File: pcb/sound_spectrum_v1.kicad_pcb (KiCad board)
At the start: 4 copper layers, 85.6 x 54 mm, 33 parts, among them IC1-L1 ICS-43432, IC2-R1 ICS-43432, J1 SWD_CONN, J2 Conn_02x10_Counter_Clockwise, P1 USB_C_Plug_USB2.0, SW2 SW_DPST_x2, U1 STM32G473CBTx, U2 AP2112K-3.3, U3 USBLC6-2SC6, Y2 SG-210STF 48.0000ML5

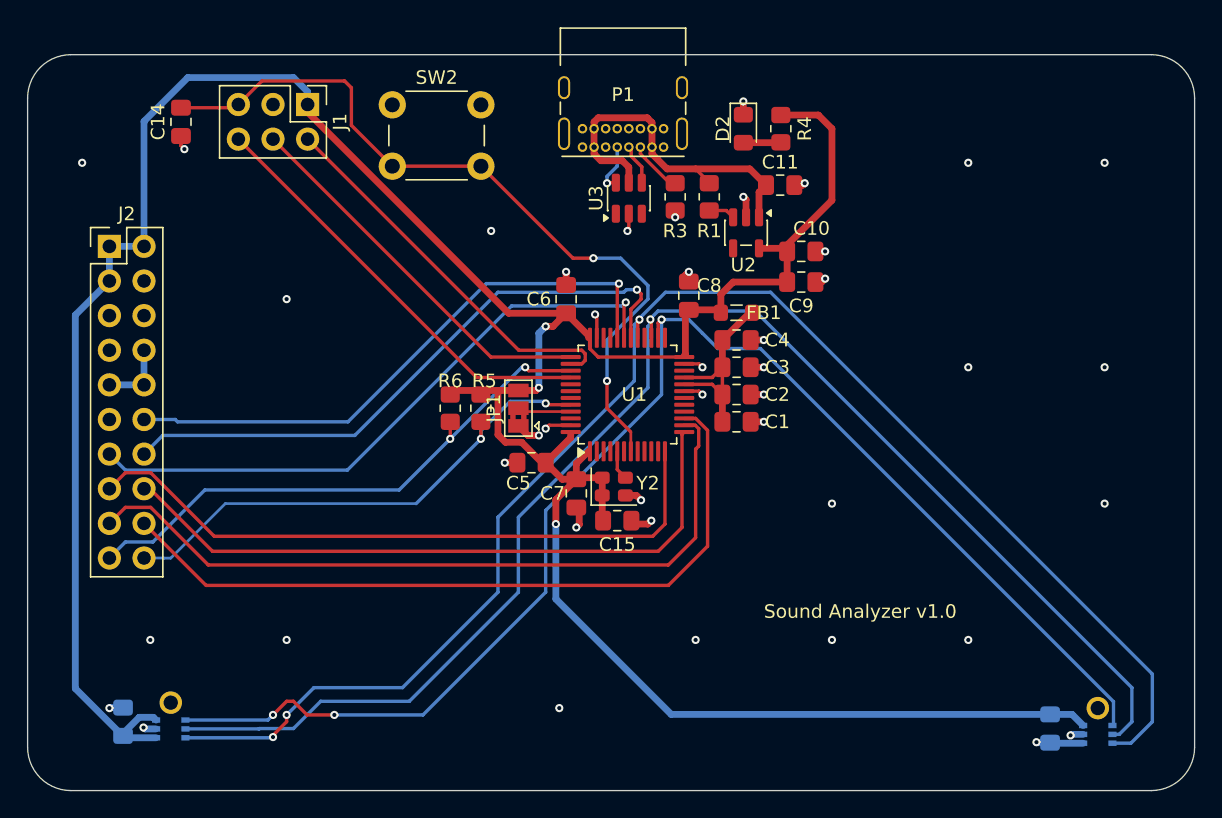
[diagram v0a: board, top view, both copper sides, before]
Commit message: feat: add mounting holes
chore: change usb c receptor

chore: align microphones
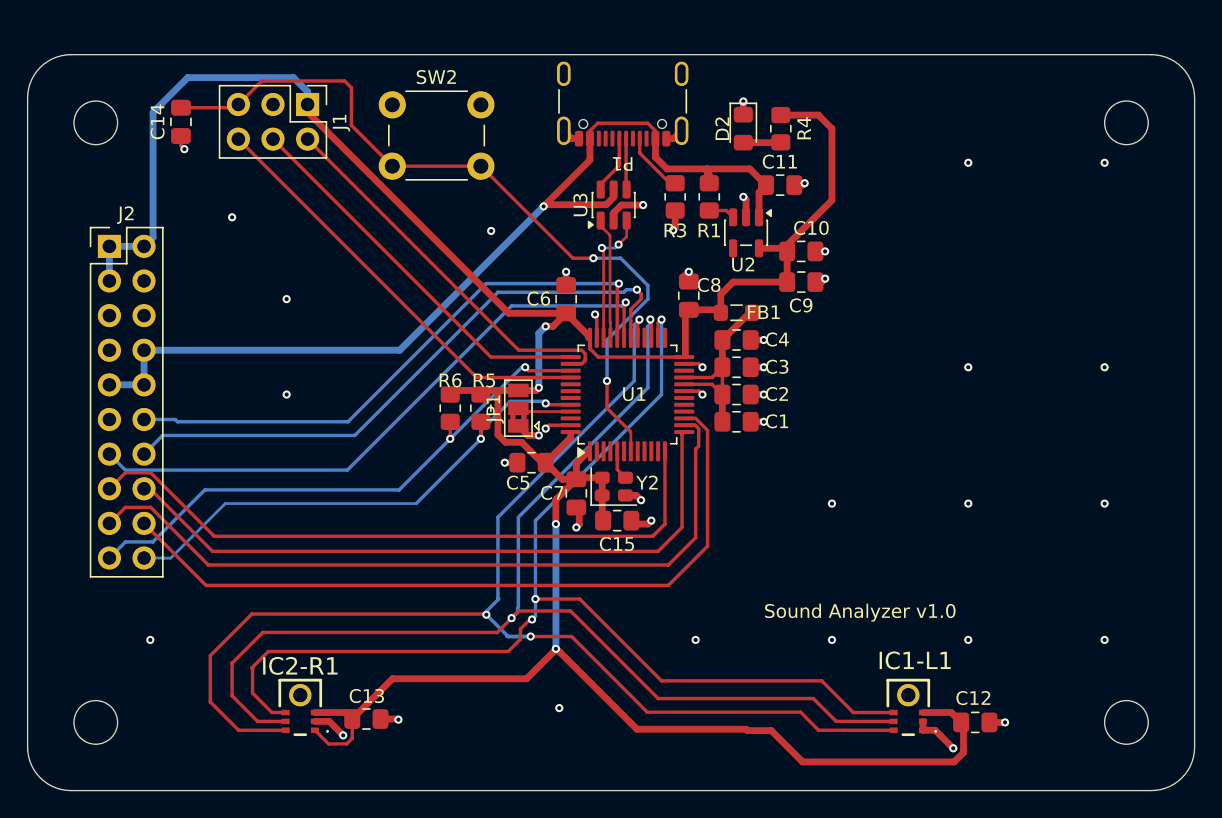
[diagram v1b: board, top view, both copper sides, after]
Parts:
- added H1: MountingHole, MountingHole:MountingHole_3.2mm_M3_DIN965, F.Cu at (181.6, 97.1)
- added H2: MountingHole, MountingHole:MountingHole_3.2mm_M3_DIN965, F.Cu at (106.0, 97.1)
- added H3: MountingHole, MountingHole:MountingHole_3.2mm_M3_DIN965, F.Cu at (181.6, 141.1)
- added H4: MountingHole, MountingHole:MountingHole_3.2mm_M3_DIN965, F.Cu at (106.0, 141.1)
- C12, C13, IC1-L1, IC2-R1: moved to F.Cu
- P1: footprint Connector_USB:USB_C_Receptacle_GCT_USB4085 -> Connector_USB:USB_C_Receptacle_GCT_USB4105-xx-A_16P_TopMnt_Horizontal
- moved C13 17.9 mm to (125.8, 140.8), turned to 0 degrees
- moved IC1-L1 13.9 mm to (165.6, 139.1)
- moved IC2-R1 9.52 mm to (121.0, 139.1)
- moved C12 5.51 mm to (170.5, 141.1), turned to 0 degrees
- moved P1 5.24 mm to (144.7, 94.5)
- moved U3 1.22 mm to (144.0, 103.1)
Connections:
- net USB_DM renamed USB_N
- net USB_DM_EXT renamed USB_EXT_N
- net USB_DP renamed USB_P
- net USB_DP_EXT renamed USB_EXT_P
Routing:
- net VBUS: track 31.7 -> 71.6 mm, vias 0 -> 1
- net I2S_WS: track 102.6 -> 84.6 mm
- net I2S_CK: track 105.3 -> 88.1 mm, vias 1 -> 2
- net +3.3V: track 240.5 -> 223.8 mm, vias 3 -> 4
- net I2S_SD: track 110.6 -> 94.3 mm
- net USB_P: track 0.00 -> 9.97 mm, vias 0 -> 2
- net USB_N: track 0.00 -> 8.90 mm
- net GND: track 33.6 -> 41.0 mm, vias 42 -> 44
- net USB_EXT_P: track 3.01 -> 4.33 mm
- net USB_EXT_N: track 3.63 -> 4.75 mm, vias 1 -> 0
- net Net-(P1-CC): track 3.94 -> 4.58 mm

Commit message: chore: minor rerouting
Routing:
- net SWCLK: track 28.5 -> 36.2 mm
- net SWO: track 31.6 -> 32.5 mm
- net GND: vias 44 -> 45

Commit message: chore: add extra led
chore: minor changes
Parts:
- removed Y2: SG-210STF 48.0000ML5, Oscillator:Oscillator_SMD_SeikoEpson_SG210-4Pin_2.5x2.0mm
- added C16: 33pF, Capacitor_SMD:C_0805_2012Metric_Pad1.18x1.45mm_HandSolder, F.Cu at (144.8, 123.5)
- added D1: LED - Green, LED_SMD:LED_0805_2012Metric_Pad1.15x1.40mm_HandSolder, F.Cu at (162.5, 97.5)
- added R2: 1k, Resistor_SMD:R_0805_2012Metric_Pad1.20x1.40mm_HandSolder, F.Cu at (165.5, 97.5)
- added Y1: ABMM2-24.000MHZ-E2-T, Samacsys:ABMM2, F.Cu at (146.8, 126.8)
- C15: value 100nF -> 33pF
- D2: value LED -> LED - Red
- FB1: value 4.7uH -> ~
- moved C15 5.49 mm to (149.0, 123.5)
- moved P1 0.85 mm to (144.7, 95.4)
- moved C12 0.41 mm to (170.1, 141.1)
- moved C13 0.35 mm to (125.5, 140.8)
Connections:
- C15 pad 1: +3.3V -> Net-(U1-PF1)
- U1 pad 25: unconnected-(U1-PB11-Pad25) -> LED_DBG
- U1 pad 6: unconnected-(U1-PF1-Pad6) -> Net-(U1-PF1)
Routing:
- net LED_DBG: track 0.00 -> 34.0 mm, vias 0 -> 2
- net GND: track 41.0 -> 48.7 mm, vias 45 -> 46
- net Net-(U1-PF1): track 0.00 -> 7.09 mm
- net SPI_MOSI: track 55.0 -> 61.7 mm
- net Net-(U1-PF0): track 2.19 -> 8.22 mm
- net SPI_MISO: track 55.3 -> 60.6 mm
- net +3.3V: track 223.9 -> 218.9 mm
- net SPI_SCK: track 49.2 -> 54.1 mm
- net Net-(D1-A): track 0.00 -> 3.85 mm
- net VBUS: track 71.6 -> 69.3 mm
- net SPI_NSS: track 48.9 -> 50.2 mm, vias 0 -> 2
- net Net-(P1-CC): track 4.58 -> 3.62 mm
- net USB_EXT_N: track 4.75 -> 3.90 mm
- net USB_EXT_P: track 4.33 -> 3.48 mm
